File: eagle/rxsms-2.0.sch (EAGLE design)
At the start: 145 parts, among them Q1 opt, Q10 BSS123, Q11 BSS123, Q12 BSS123, Q2 BSS123, Q3 BSS123, Q4 BSS123, Q5 BSS123, Q6 BSS123, Q7 BSS123, Q8 BSS123, Q9 BSS123, T1 SMS_IP67, T10 SWITCH_LED, T2 SMS_IP67, T3 SWITCH_LED, T4 SMS_IP67, T5 SMS_IP67, T6 SWITCH_LED, T7 SWITCH_LED, T8 SWITCH_LED, T9 SMS_IP67, U1 MAX3232ESE, U2 XMEGA-A4UTQFP, U3 TSR_1-2450, U4 LM1117, U5 TMV_0505EN, U6 ADUM3160, U7 TPS73125, U8 NUP2202W1, X1 PN61729-S, X5 RLP2-200-500

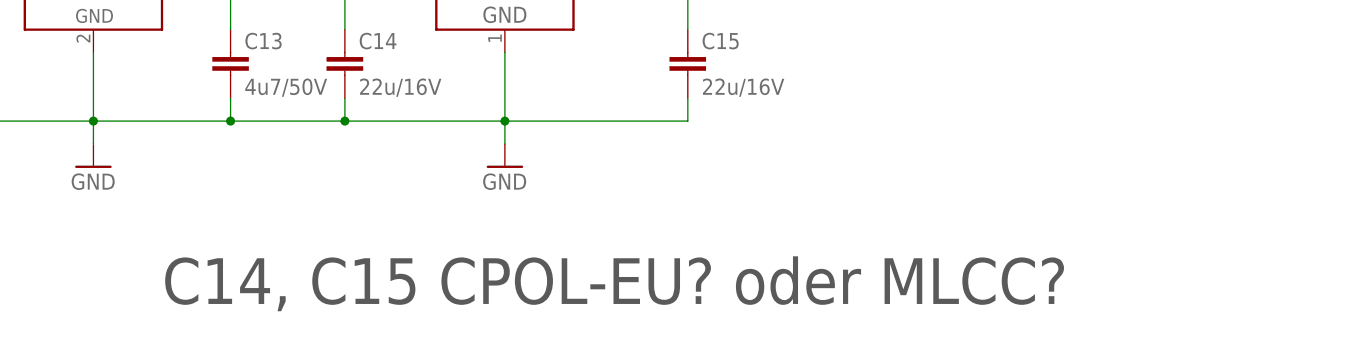
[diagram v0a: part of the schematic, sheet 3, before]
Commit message: remove note/TODO; decide to use MLCC capacitor for LD1117
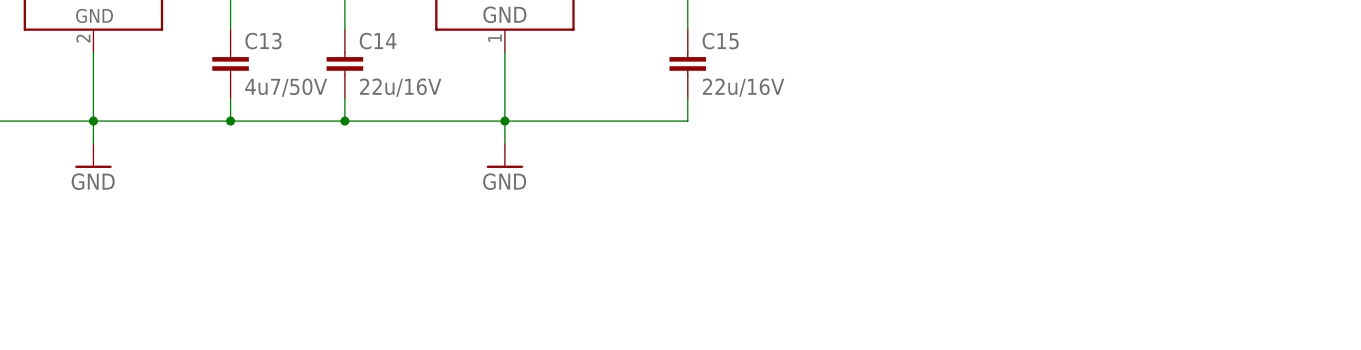
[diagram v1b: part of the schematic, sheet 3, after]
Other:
- note removed: "C14, C15 CPOL-EU? oder MLCC?"
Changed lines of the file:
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@@
 <sheet>
 <plain>
-<text x="86.36" y="88.9" size="5.08" layer="97">C14, C15 CPOL-EU? oder MLCC?</text>
 <text x="27.94" y="152.4" size="5.08" layer="97">TODO Schraubklemmen, Inductor</text>
 </plain>

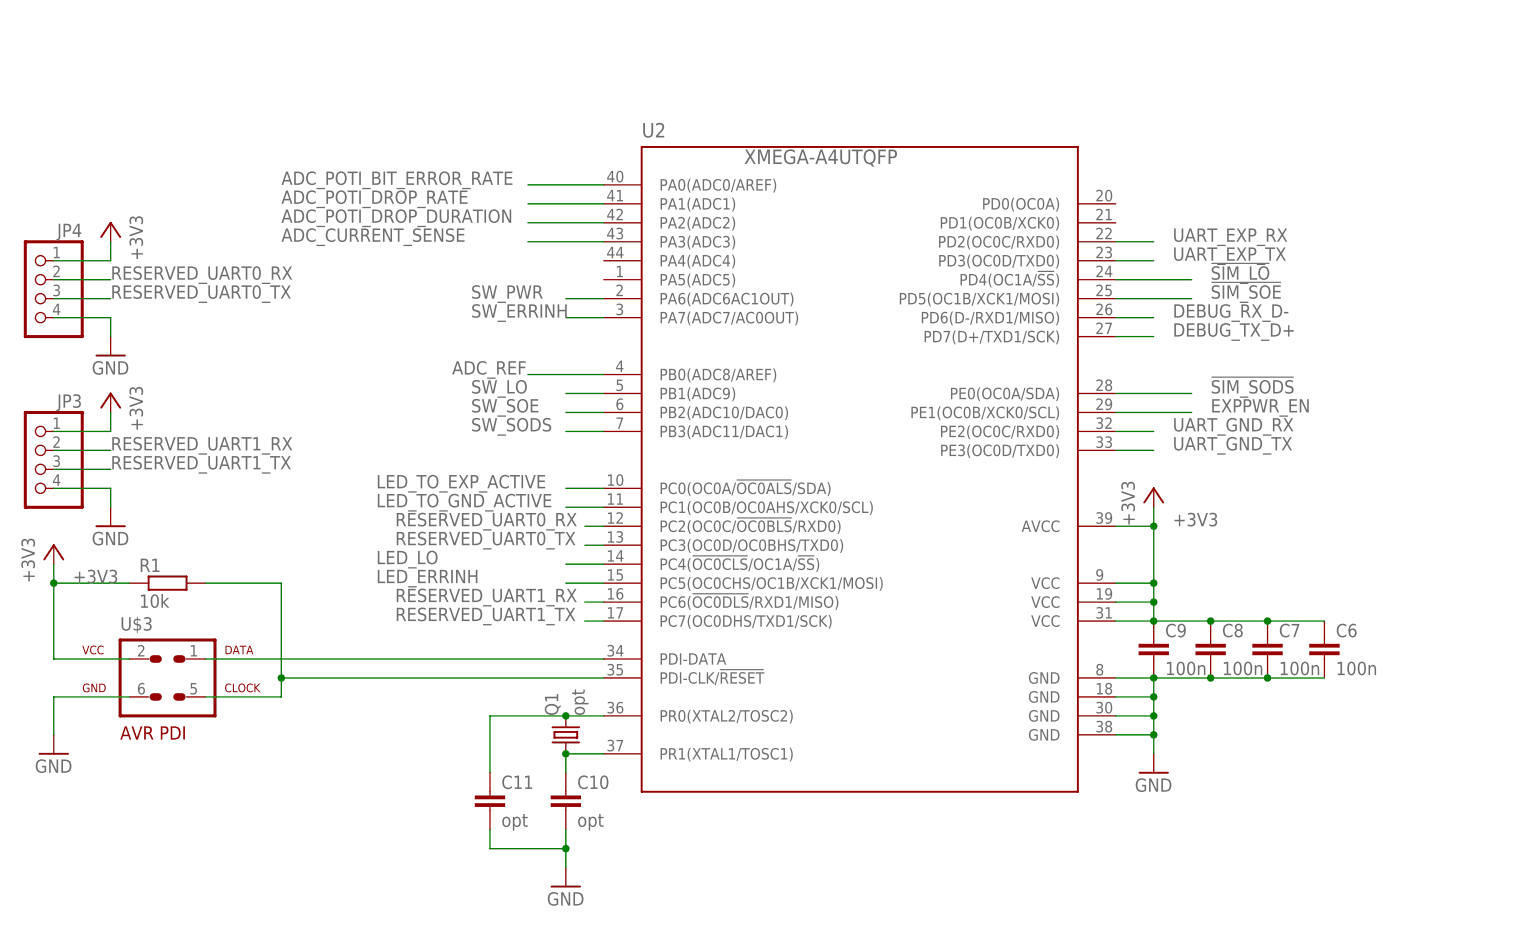
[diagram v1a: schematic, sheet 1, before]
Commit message: reordered signals on uC
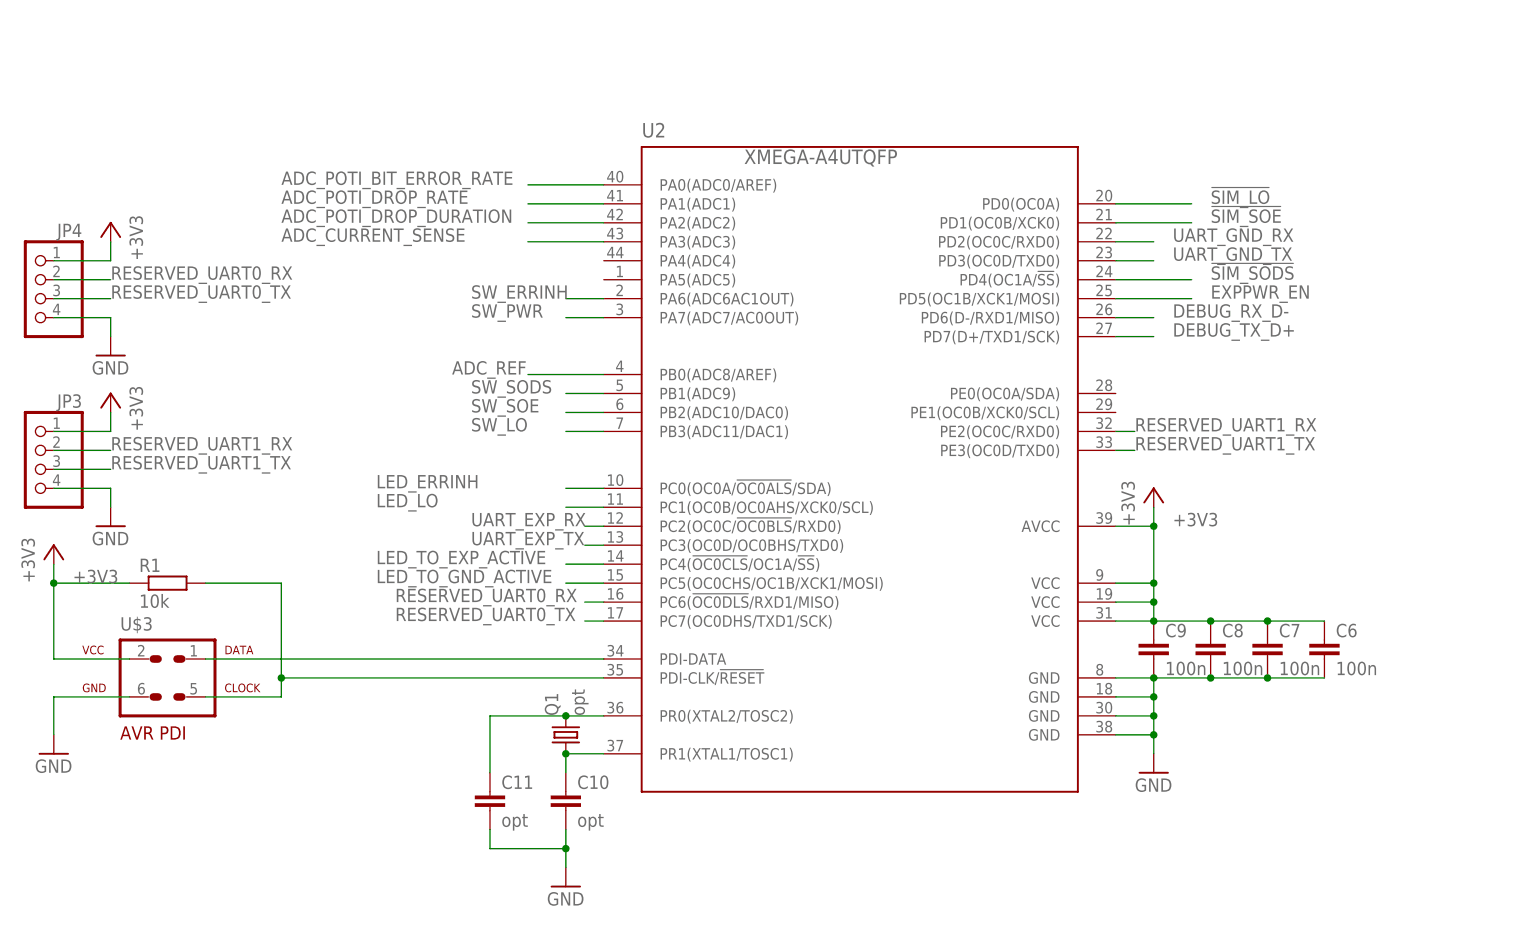
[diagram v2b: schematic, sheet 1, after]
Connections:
- net !SIM_LO: no longer U2.PD4(OC1A/!SS!)
- net !SIM_SODS: no longer U2.PE0(OC0A/SDA)
- net !SIM_SOE: no longer U2.PD5(OC1B/XCK1/MOSI)
- net DEBUG_RX_D-: no longer U2.PD6(D-/RXD1/MISO)
- net DEBUG_TX_D+: no longer U2.PD7(D+/TXD1/SCK)
- net EXPPWR_EN: no longer U2.PE1(OC0B/XCK0/SCL)
- net LED_ERRINH: no longer U2.PC5(OC0CHS/OC1B/XCK1/MOSI)
- net LED_LO: no longer U2.PC4(!OC0CLS!/OC1A/!SS!)
- net LED_TO_EXP_ACTIVE: no longer U2.PC0(OC0A/!OC0ALS!/SDA)
- net LED_TO_GND_ACTIVE: no longer U2.PC1(OC0B/OC0AHS/XCK0/SCL)
- net RESERVED_UART0_RX: no longer U2.PC2(OC0C/!OC0BLS!/RXD0)
- net RESERVED_UART0_TX: no longer U2.PC3(OC0D/OC0BHS/TXD0)
- net RESERVED_UART1_RX: no longer U2.PC6(!OC0DLS!/RXD1/MISO)
- net RESERVED_UART1_TX: no longer U2.PC7(OC0DHS/TXD1/SCK)
- net SW_ERRINH: no longer U2.PA7(ADC7/AC0OUT)
- net SW_LO: now also U2.PB3(ADC11/DAC1); no longer U2.PB1(ADC9)
- net SW_PWR: no longer U2.PA6(ADC6AC1OUT)
- net SW_SODS: now also U2.PB1(ADC9); no longer U2.PB3(ADC11/DAC1)
- net UART_EXP_RX: no longer U2.PD2(OC0C/RXD0)
- net UART_EXP_TX: no longer U2.PD3(OC0D/TXD0)
- net UART_GND_RX: no longer U2.PE2(OC0C/RXD0)
- net UART_GND_TX: no longer U2.PE3(OC0D/TXD0)
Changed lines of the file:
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@@
 <net name="DEBUG_RX_D-" class="0">
 <segment>
-<pinref part="U2" gate="G$1" pin="PD6(D-/RXD1/MISO)"/>
 <wire x1="157.48" y1="121.92" x2="162.56" y2="121.92" width="0.1524" layer="91"/>
 <label x="165.1" y="121.92" size="1.778" layer="95"/>
@@
 <net name="DEBUG_TX_D+" class="0">
 <segment>
-<pinref part="U2" gate="G$1" pin="PD7(D+/TXD1/SCK)"/>
 <wire x1="157.48" y1="119.38" x2="162.56" y2="119.38" width="0.1524" layer="91"/>
 <label x="165.1" y="119.38" size="1.778" layer="95"/>
@@
 <net name="UART_GND_TX" class="0">
 <segment>
-<pinref part="U2" gate="G$1" pin="PE3(OC0D/TXD0)"/>
-<wire x1="157.48" y1="104.14" x2="162.56" y2="104.14" width="0.1524" layer="91"/>
-<label x="165.1" y="104.14" size="1.778" layer="95"/>
+<wire x1="157.48" y1="129.54" x2="162.56" y2="129.54" width="0.1524" layer="91"/>
+<label x="165.1" y="129.54" size="1.778" layer="95"/>
 </segment>
 </net>
 <net name="UART_GND_RX" class="0">
 <segment>
-<pinref part="U2" gate="G$1" pin="PE2(OC0C/RXD0)"/>
-<wire x1="157.48" y1="106.68" x2="162.56" y2="106.68" width="0.1524" layer="91"/>
-<label x="165.1" y="106.68" size="1.778" layer="95"/>
+<wire x1="157.48" y1="132.08" x2="162.56" y2="132.08" width="0.1524" layer="91"/>
+<label x="165.1" y="132.08" size="1.778" layer="95"/>
 </segment>
 </net>
 <net name="UART_EXP_RX" class="0">
 <segment>
-<pinref part="U2" gate="G$1" pin="PD2(OC0C/RXD0)"/>
-<wire x1="157.48" y1="132.08" x2="162.56" y2="132.08" width="0.1524" layer="91"/>
-<label x="165.1" y="132.08" size="1.778" layer="95"/>
+<wire x1="88.9" y1="93.98" x2="86.36" y2="93.98" width="0.1524" layer="91"/>
+<label x="71.12" y="93.98" size="1.778" layer="95"/>
 </segment>
 </net>
 <net name="UART_EXP_TX" class="0">
 <segment>
-<pinref part="U2" gate="G$1" pin="PD3(OC0D/TXD0)"/>
-<wire x1="157.48" y1="129.54" x2="162.56" y2="129.54" width="0.1524" layer="91"/>
-<label x="165.1" y="129.54" size="1.778" layer="95"/>
+<wire x1="88.9" y1="91.44" x2="86.36" y2="91.44" width="0.1524" layer="91"/>
+<label x="71.12" y="91.44" size="1.778" layer="95"/>
 </segment>
 </net>
@@
 </segment>
 <segment>
-<pinref part="U2" gate="G$1" pin="PC2(OC0C/!OC0BLS!/RXD0)"/>
-<wire x1="88.9" y1="93.98" x2="86.36" y2="93.98" width="0.1524" layer="91"/>
-<label x="60.96" y="93.98" size="1.778" layer="95"/>
+<wire x1="88.9" y1="83.82" x2="86.36" y2="83.82" width="0.1524" layer="91"/>
+<label x="60.96" y="83.82" size="1.778" layer="95"/>
 </segment>
 </net>
@@
 </segment>
 <segment>
-<pinref part="U2" gate="G$1" pin="PC3(OC0D/OC0BHS/TXD0)"/>
-<wire x1="88.9" y1="91.44" x2="86.36" y2="91.44" width="0.1524" layer="91"/>
-<label x="60.96" y="91.44" size="1.778" layer="95"/>
+<wire x1="88.9" y1="81.28" x2="86.36" y2="81.28" width="0.1524" layer="91"/>
+<label x="60.96" y="81.28" size="1.778" layer="95"/>
 </segment>
 </net>
@@
 </segment>
 <segment>
-<pinref part="U2" gate="G$1" pin="PC6(!OC0DLS!/RXD1/MISO)"/>
-<wire x1="88.9" y1="83.82" x2="86.36" y2="83.82" width="0.1524" layer="91"/>
-<label x="60.96" y="83.82" size="1.778" layer="95"/>
+<wire x1="160.02" y1="106.68" x2="157.48" y2="106.68" width="0.1524" layer="91"/>
+<label x="160.02" y="106.68" size="1.778" layer="95"/>
 </segment>
 </net>
@@
 </segment>
 <segment>
-<pinref part="U2" gate="G$1" pin="PC7(OC0DHS/TXD1/SCK)"/>
-<wire x1="88.9" y1="81.28" x2="86.36" y2="81.28" width="0.1524" layer="91"/>
-<label x="60.96" y="81.28" size="1.778" layer="95"/>
+<wire x1="160.02" y1="104.14" x2="157.48" y2="104.14" width="0.1524" layer="91"/>
+<label x="160.02" y="104.14" size="1.778" layer="95"/>
 </segment>
 </net>
 <net name="!SIM_SODS" class="0">
 <segment>
-<pinref part="U2" gate="G$1" pin="PE0(OC0A/SDA)"/>
-<wire x1="157.48" y1="111.76" x2="167.64" y2="111.76" width="0.1524" layer="91"/>
-<label x="170.18" y="111.76" size="1.778" layer="95"/>
+<wire x1="157.48" y1="127" x2="167.64" y2="127" width="0.1524" layer="91"/>
+<label x="170.18" y="127" size="1.778" layer="95"/>
 </segment>
 </net>
 <net name="EXPPWR_EN" class="0">
 <segment>
-<pinref part="U2" gate="G$1" pin="PE1(OC0B/XCK0/SCL)"/>
-<wire x1="157.48" y1="109.22" x2="167.64" y2="109.22" width="0.1524" layer="91"/>
-<label x="170.18" y="109.22" size="1.778" layer="95"/>
+<wire x1="157.48" y1="124.46" x2="167.64" y2="124.46" width="0.1524" layer="91"/>
+<label x="170.18" y="124.46" size="1.778" layer="95"/>
 </segment>
 </net>
 <net name="!SIM_SOE" class="0">
 <segment>
-<pinref part="U2" gate="G$1" pin="PD5(OC1B/XCK1/MOSI)"/>
-<wire x1="157.48" y1="124.46" x2="167.64" y2="124.46" width="0.1524" layer="91"/>
-<label x="170.18" y="124.46" size="1.778" layer="95"/>
+<wire x1="157.48" y1="134.62" x2="167.64" y2="134.62" width="0.1524" layer="91"/>
+<label x="170.18" y="134.62" size="1.778" layer="95"/>
 </segment>
 </net>
 <net name="!SIM_LO" class="0">
 <segment>
-<pinref part="U2" gate="G$1" pin="PD4(OC1A/!SS!)"/>
-<wire x1="157.48" y1="127" x2="167.64" y2="127" width="0.1524" layer="91"/>
-<label x="170.18" y="127" size="1.778" layer="95"/>
+<wire x1="157.48" y1="137.16" x2="167.64" y2="137.16" width="0.1524" layer="91"/>
+<label x="170.18" y="137.16" size="1.778" layer="95"/>
 </segment>
 </net>
 <net name="SW_PWR" class="0">
 <segment>
-<pinref part="U2" gate="G$1" pin="PA6(ADC6AC1OUT)"/>
-<wire x1="88.9" y1="124.46" x2="83.82" y2="124.46" width="0.1524" layer="91"/>
-<label x="71.12" y="124.46" size="1.778" layer="95"/>
+<wire x1="88.9" y1="121.92" x2="83.82" y2="121.92" width="0.1524" layer="91"/>
+<label x="71.12" y="121.92" size="1.778" layer="95"/>
 </segment>
 </net>
 <net name="SW_ERRINH" class="0">
 <segment>
-<pinref part="U2" gate="G$1" pin="PA7(ADC7/AC0OUT)"/>
-<wire x1="88.9" y1="121.92" x2="83.82" y2="121.92" width="0.1524" layer="91"/>
-<label x="71.12" y="121.92" size="1.778" layer="95"/>
-</segment>
-</net>
-<net name="SW_LO" class="0">
-<segment>
-<pinref part="U2" gate="G$1" pin="PB1(ADC9)"/>
-<wire x1="88.9" y1="111.76" x2="83.82" y2="111.76" width="0.1524" layer="91"/>
-<label x="71.12" y="111.76" size="1.778" layer="95"/>
+<wire x1="88.9" y1="124.46" x2="83.82" y2="124.46" width="0.1524" layer="91"/>
+<label x="71.12" y="124.46" size="1.778" layer="95"/>
 </segment>
 </net>
@@
 </segment>
 </net>
+<net name="LED_TO_EXP_ACTIVE" class="0">
+<segment>
+<wire x1="88.9" y1="88.9" x2="83.82" y2="88.9" width="0.1524" layer="91"/>
+<label x="58.42" y="88.9" size="1.778" layer="95"/>
+</segment>
+</net>
+<net name="LED_TO_GND_ACTIVE" class="0">
+<segment>
+<wire x1="88.9" y1="86.36" x2="83.82" y2="86.36" width="0.1524" layer="91"/>
+<label x="58.42" y="86.36" size="1.778" layer="95"/>
+</segment>
+</net>
+<net name="LED_LO" class="0">
+<segment>
+<wire x1="88.9" y1="96.52" x2="83.82" y2="96.52" width="0.1524" layer="91"/>
+<label x="58.42" y="96.52" size="1.778" layer="95"/>
+</segment>
+</net>
+<net name="LED_ERRINH" class="0">
+<segment>
+<wire x1="88.9" y1="99.06" x2="83.82" y2="99.06" width="0.1524" layer="91"/>
+<label x="58.42" y="99.06" size="1.778" layer="95"/>
+</segment>
+</net>
 <net name="SW_SODS" class="0">
+<segment>
+<pinref part="U2" gate="G$1" pin="PB1(ADC9)"/>
+<wire x1="88.9" y1="111.76" x2="83.82" y2="111.76" width="0.1524" layer="91"/>
+<label x="71.12" y="111.76" size="1.778" layer="95"/>
+</segment>
+</net>
+<net name="SW_LO" class="0">
 <segment>
 <pinref part="U2" gate="G$1" pin="PB3(ADC11/DAC1)"/>
@@
 </segment>
 </net>
-<net name="LED_TO_EXP_ACTIVE" class="0">
-<segment>
-<pinref part="U2" gate="G$1" pin="PC0(OC0A/!OC0ALS!/SDA)"/>
-<wire x1="88.9" y1="99.06" x2="83.82" y2="99.06" width="0.1524" layer="91"/>
-<label x="58.42" y="99.06" size="1.778" layer="95"/>
-</segment>
-</net>
-<net name="LED_TO_GND_ACTIVE" class="0">
-<segment>
-<pinref part="U2" gate="G$1" pin="PC1(OC0B/OC0AHS/XCK0/SCL)"/>
-<wire x1="88.9" y1="96.52" x2="83.82" y2="96.52" width="0.1524" layer="91"/>
-<label x="58.42" y="96.52" size="1.778" layer="95"/>
-</segment>
-</net>
-<net name="LED_LO" class="0">
-<segment>
-<pinref part="U2" gate="G$1" pin="PC4(!OC0CLS!/OC1A/!SS!)"/>
-<wire x1="88.9" y1="88.9" x2="83.82" y2="88.9" width="0.1524" layer="91"/>
-<label x="58.42" y="88.9" size="1.778" layer="95"/>
-</segment>
-</net>
-<net name="LED_ERRINH" class="0">
-<segment>
-<pinref part="U2" gate="G$1" pin="PC5(OC0CHS/OC1B/XCK1/MOSI)"/>
-<wire x1="88.9" y1="86.36" x2="83.82" y2="86.36" width="0.1524" layer="91"/>
-<label x="58.42" y="86.36" size="1.778" layer="95"/>
-</segment>
-</net>
